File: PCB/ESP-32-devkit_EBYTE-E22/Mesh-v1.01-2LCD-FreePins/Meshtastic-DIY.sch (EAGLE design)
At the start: 24 parts

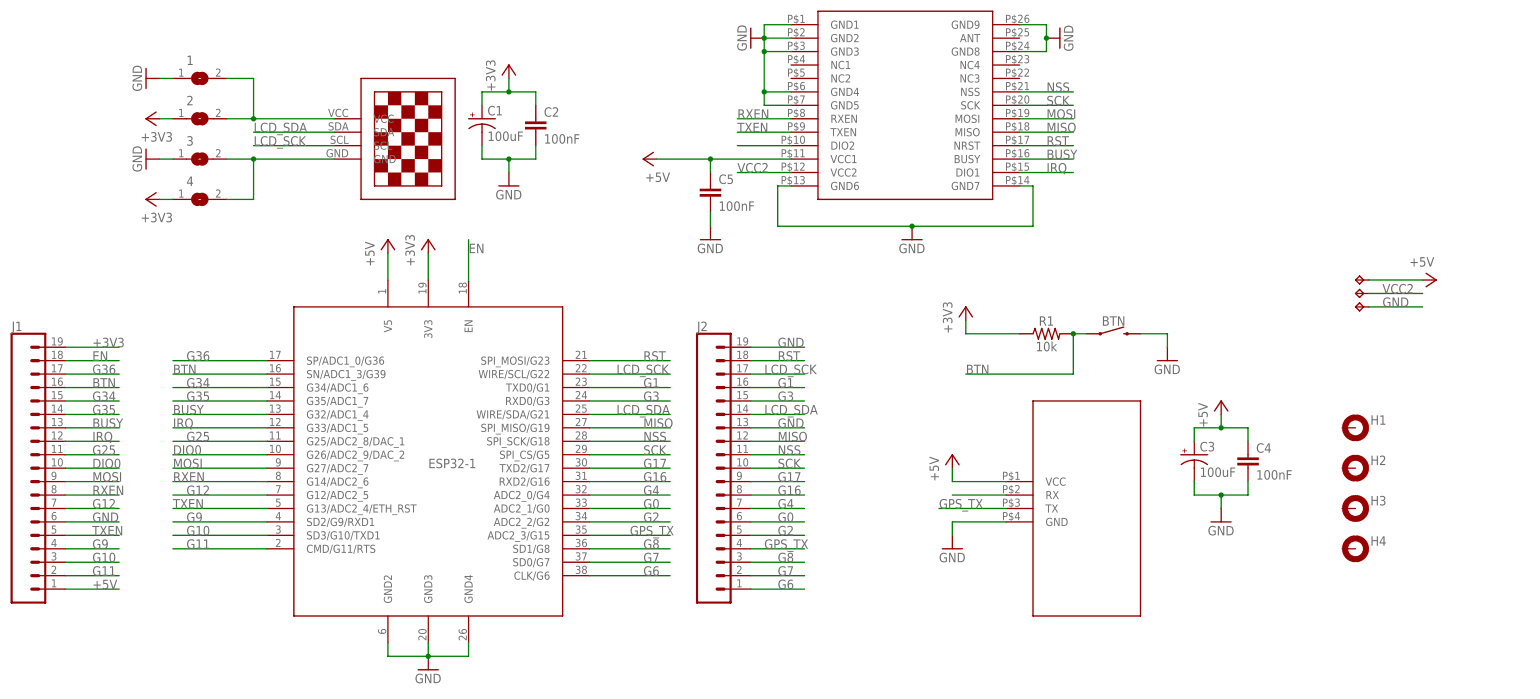
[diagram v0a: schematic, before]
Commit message: PCB updates (#15)
* fixes PCB version and description

* Updated revision of the v1.01 PCB

* Fixed drill layout for v.1.05

* Updated EBYTE E22 adapter (removed excessive antenna line)

* Updated PCB v1.03

* Updated PCB v1.02

* Removed untested PCB design

* [PCB] Missing brd&sch for 1.01 & updated 1.02

* v1.04 update

* [PCB] Meshtastic-DIY_v1.06 - TTGO T-Energy T18 V3.0 HAT
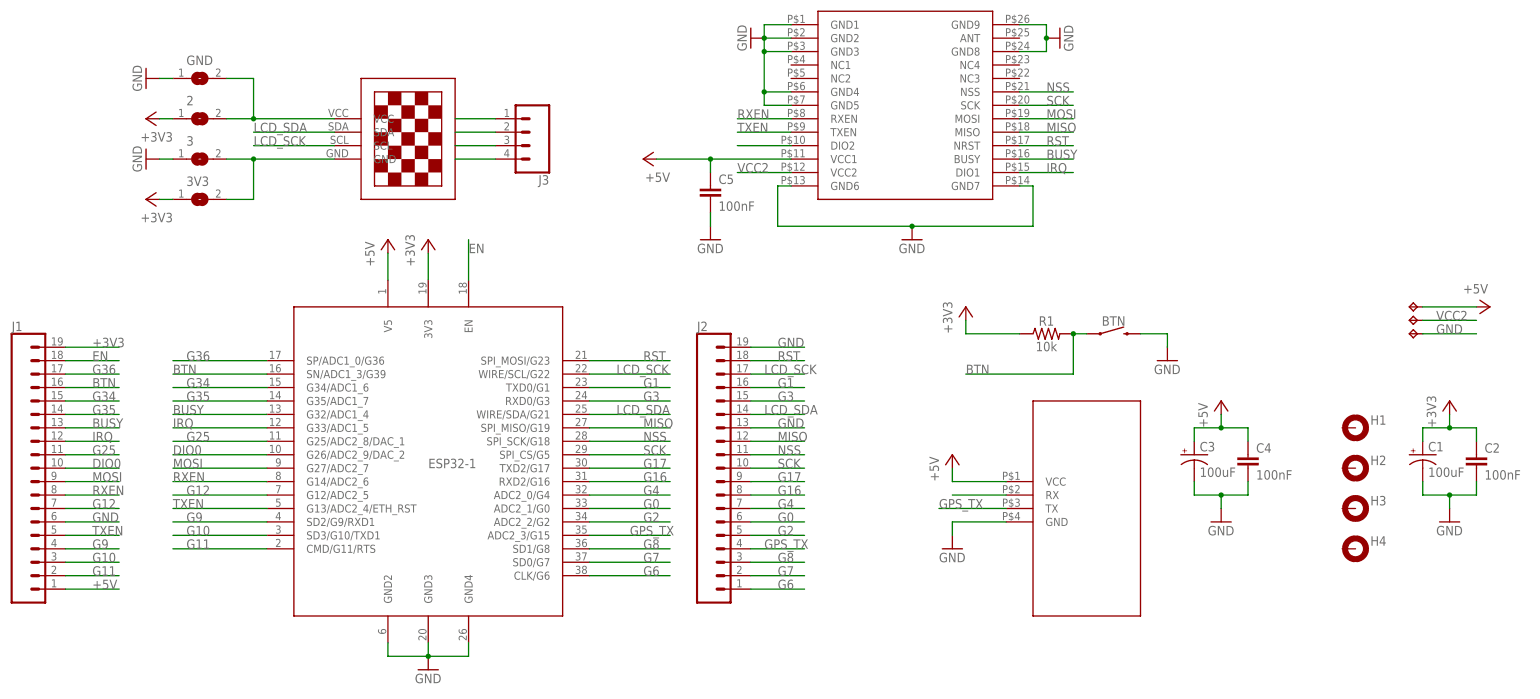
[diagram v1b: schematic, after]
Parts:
- added J3: (no value), SparkFun-Connectors:CONN_041X04_NO_SILK
- renumbered 1 to GND, 4 to 3V3
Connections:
- net LCD_SCK: now also J3.3
- net LCD_SDA: now also J3.4
- net N$2: now also J3.2
- net N$4: now also J3.1
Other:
- moved on the sheet: C1, C2
